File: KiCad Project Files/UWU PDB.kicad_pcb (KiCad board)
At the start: 4 copper layers, 96.5 x 92.2 mm, 73 parts, among them J1 XT90, J10 XT60 ESC, J11 PWM ESC, J12 PWM ESC, J13 PWM ESC, J14 PWM ESC, J15 PWM ESC, J16 PWM ESC, J17 PWM ESC, J18 PWM ESC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

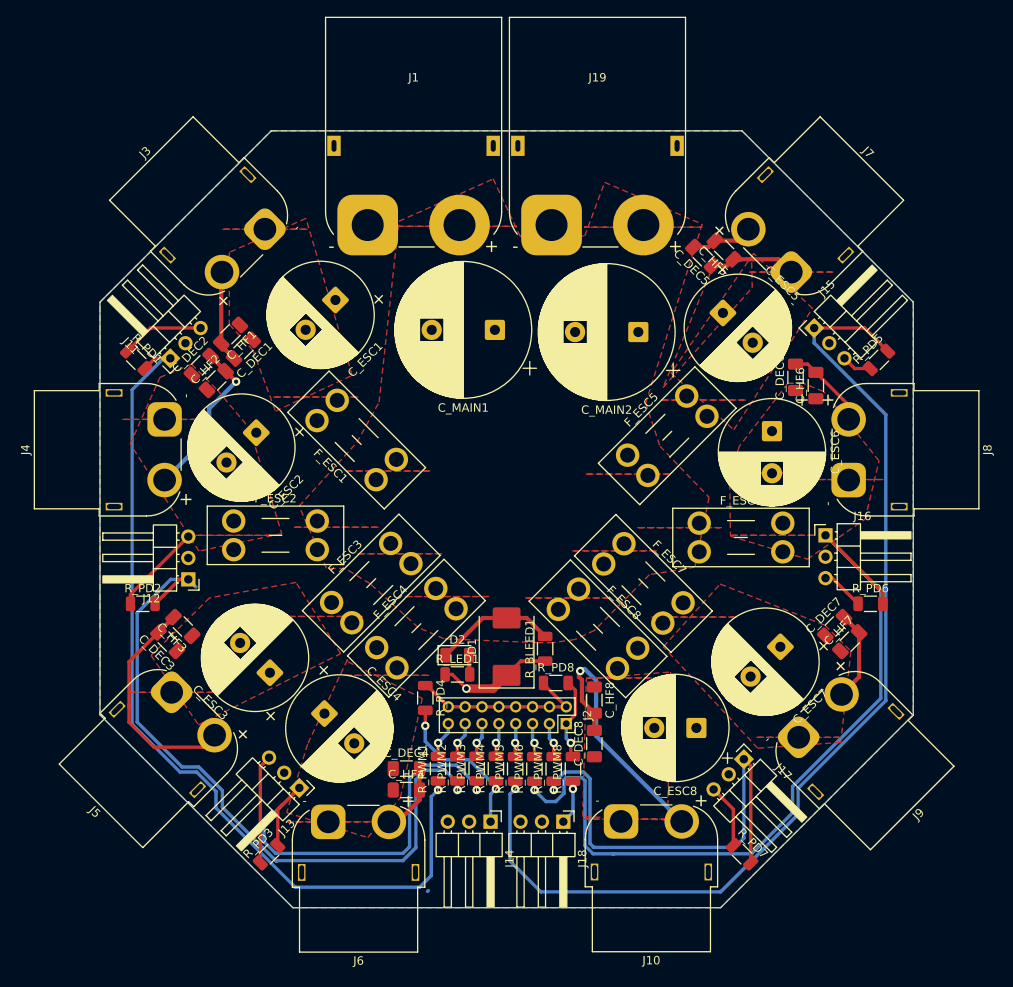
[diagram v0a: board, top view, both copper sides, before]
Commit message: Update KiCad design files and refresh screenshots
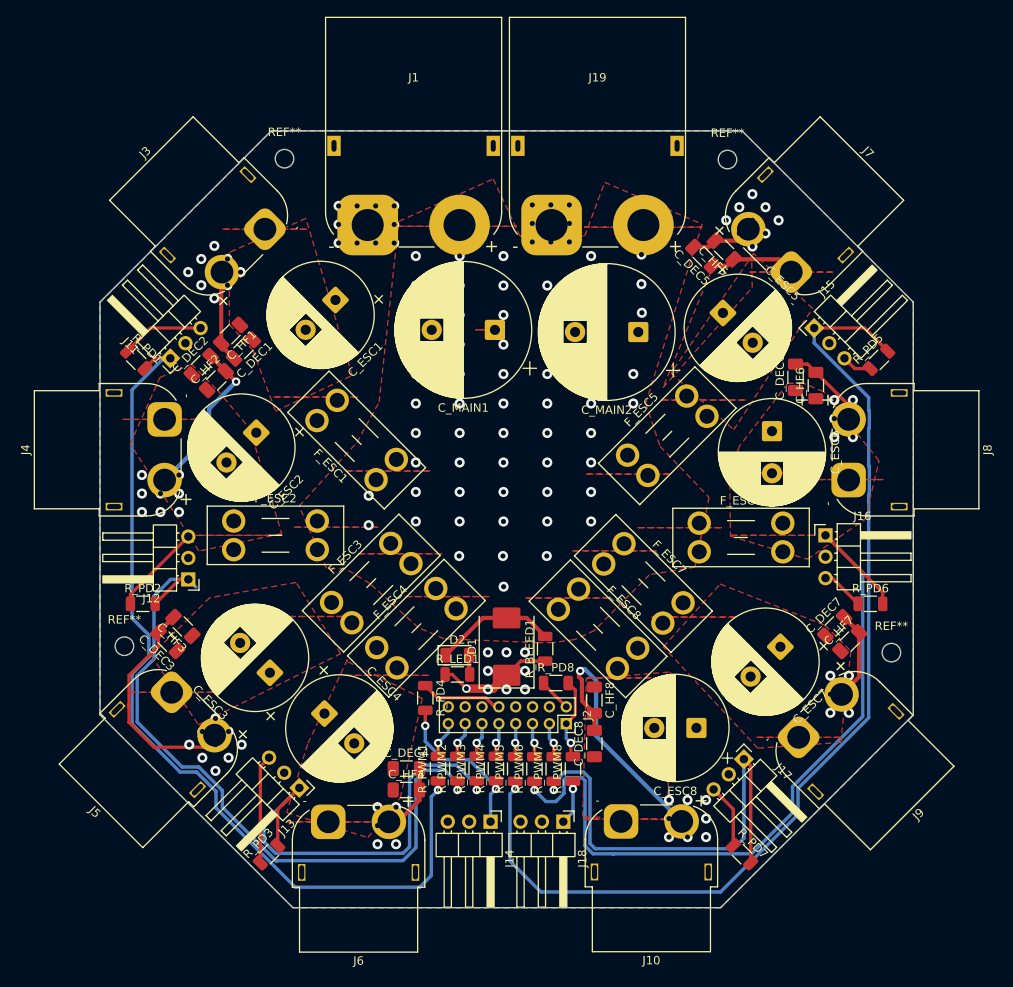
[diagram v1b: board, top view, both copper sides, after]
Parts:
- added REF**: MountingHole_2.2mm_M2, MountingHole:MountingHole_2.2mm_M2, F.Cu at (155.8, 54.2)
- added REF**: MountingHole_2.2mm_M2, MountingHole:MountingHole_2.2mm_M2, F.Cu at (103.2, 54.1)
- added REF**: MountingHole_2.2mm_M2, MountingHole:MountingHole_2.2mm_M2, F.Cu at (84.2, 112.0)
- added REF**: MountingHole_2.2mm_M2, MountingHole:MountingHole_2.2mm_M2, F.Cu at (175.2, 112.7)
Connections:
- net /con1 renamed /PWM1
- net /con11 renamed /PWM6
- net /con13 renamed /PWM7
- net /con15 renamed /PWM8
- net /con3 renamed /PWM2
- net /con5 renamed /PWM3
- net /con7 renamed /PWM4
- net /con9 renamed /PWM5
- J11 pad 3: /GND -> /PWM1G
- J12 pad 3: /GND -> /PWM2G
- J13 pad 3: /GND -> /PWM3G
- J14 pad 3: /GND -> /PWM4G
- J15 pad 3: /GND -> /PWM5G
- J16 pad 3: /GND -> /PWM6G
- J17 pad 3: /GND -> /PWM7G
- J18 pad 3: /GND -> /PWM8G
- J2 pad 10: /GND -> /PWM4G
- J2 pad 12: /GND -> /PWM3G
- J2 pad 14: /GND -> /PWM2G
- J2 pad 16: /GND -> /PWM1G
- J2 pad 2: /GND -> /PWM8G
- J2 pad 4: /GND -> /PWM7G
- J2 pad 6: /GND -> /PWM6G
- J2 pad 8: /GND -> /PWM5G
- R_PD1 pad 1: /GND -> /PWM1G
- R_PD2 pad 1: /GND -> /PWM2G
- R_PD3 pad 1: /GND -> /PWM3G
- R_PD4 pad 1: /GND -> /PWM4G
- R_PD5 pad 1: /GND -> /PWM5G
- R_PD6 pad 1: /GND -> /PWM6G
- R_PD7 pad 1: /GND -> /PWM7G
- R_PD8 pad 1: /GND -> /PWM8G
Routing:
- net /PWM1G: track 0.00 -> 129.9 mm
- net /PWM5G: track 0.00 -> 121.2 mm
- net /PWM2G: track 0.00 -> 99.3 mm
- net /PWM6G: track 0.00 -> 95.0 mm
- net /GND: track 210.5 -> 138.9 mm, vias 3 -> 95
- net /PWM3G: track 0.00 -> 67.1 mm
- net /PWM7G: track 0.00 -> 54.2 mm
- net /PWM4G: track 0.00 -> 26.1 mm
- net /PWM8G: track 0.00 -> 21.0 mm
- net /VBAT+: track 24.9 -> 27.2 mm, vias 0 -> 60
- net /PWM6: track 99.8 -> 98.0 mm
- net /PWM5: track 128.6 -> 127.0 mm
- net /PWM1: track 110.6 -> 112.1 mm
